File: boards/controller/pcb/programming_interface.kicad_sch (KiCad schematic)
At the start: 1 part, among them J14001 Conn_ST_STDC14

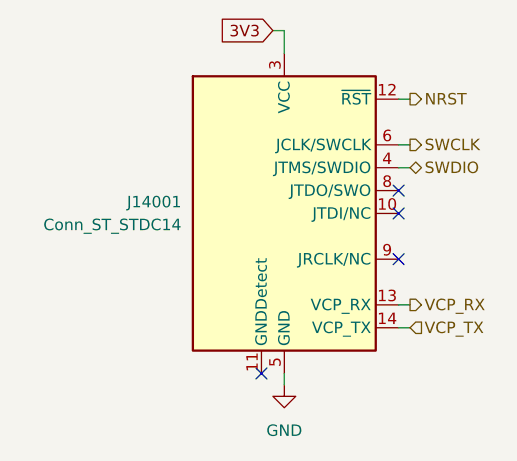
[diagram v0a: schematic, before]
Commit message: controller: Update BOM
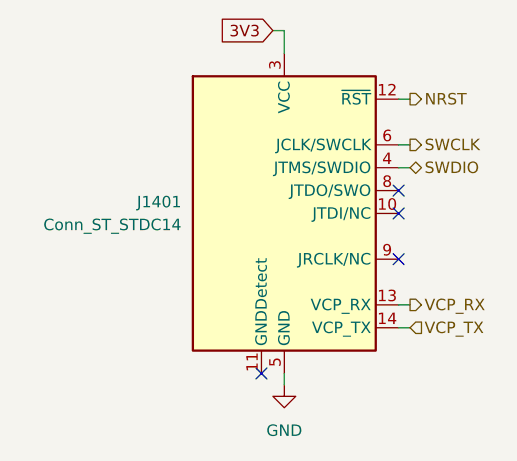
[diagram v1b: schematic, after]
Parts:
- renumbered J14001 to J1401
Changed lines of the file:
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@@
 		(dnp no)
 		(fields_autoplaced yes)
-		(property "Reference" "#PWR014001"
+		(property "Reference" "#PWR01401"
 			(at 146.05 129.54 0)
 			(effects
@@
 			(project ""
 				(path "/5caba13a-97ae-46d4-856f-900b12012fd8/1aa8928e-de08-43c0-8f11-01546d826b5e"
-					(reference "#PWR014001")
+					(reference "#PWR01401")
 					(unit 1)
 				)
@@
 		(dnp no)
 		(fields_autoplaced yes)
-		(property "Reference" "J14001"
+		(property "Reference" "J1401"
 			(at 134.62 102.8699 0)
 			(effects
@@
 			(project ""
 				(path "/5caba13a-97ae-46d4-856f-900b12012fd8/1aa8928e-de08-43c0-8f11-01546d826b5e"
-					(reference "J14001")
+					(reference "J1401")
 					(unit 1)
 				)
